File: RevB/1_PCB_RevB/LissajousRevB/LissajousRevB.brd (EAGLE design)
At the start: 99.1 x 66 mm, 77 parts, among them U101 LM348D, U201 LM348D, U401 LM348D

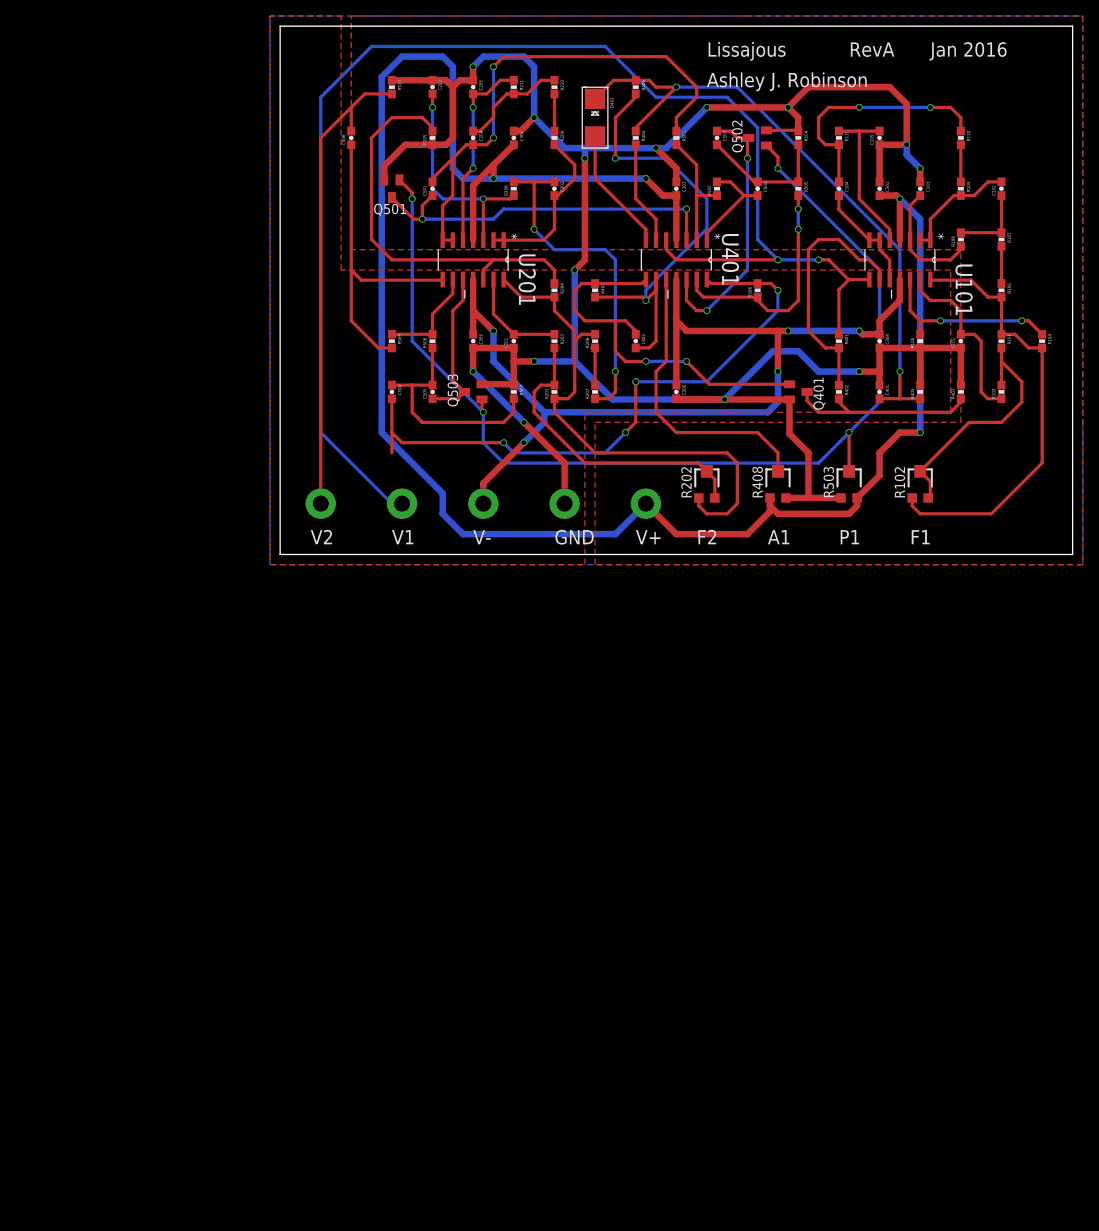
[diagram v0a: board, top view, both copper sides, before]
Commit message: down to one quad op-amp package
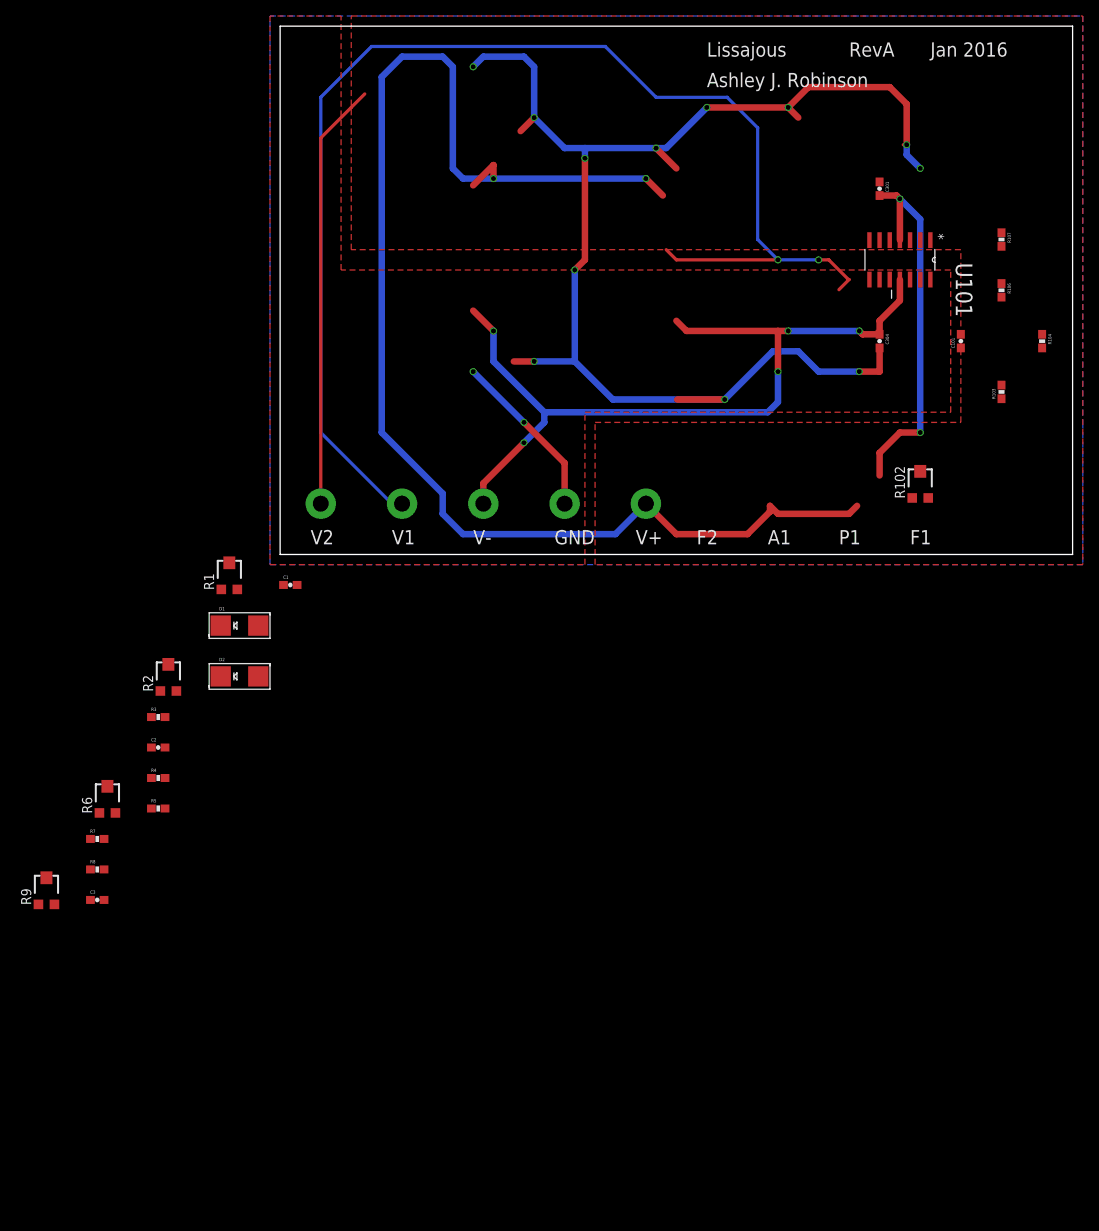
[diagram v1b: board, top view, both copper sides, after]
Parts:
- removed C102, C103, C104, C105, C201, C202, C203, C204, C205: 4.7nF, passives:0603-CAP
- removed C302, C303, C305, C306, C402: 100nF, passives:0603-CAP
- removed C401: 100pF, passives:0603-CAP
- removed C501, C502, C503, C504, C505, C506: 10nF, passives:0603-CAP
- removed D401: 1N4148, adafruit:SMADIODE
- removed Q401, Q501, Q502, Q503: (no value), adafruit:SOT23
- removed R101, R201, R403, R405, R407: DNF, passives:0603-RES
- removed R105, R108, R110, R111, R204, R205, R207, R208, R210, R211, R501, R502, R504, R505, R506, R507, R508, R509, R510: 33K, passives:0603-RES
- removed R109, R206, R209, R402: 0R, passives:0603-RES
- removed R202, R408, R503: 200K, adafruit:TC33X
- removed R203, R406: 5K6, passives:0603-RES
- removed R401: 1M, passives:0603-RES
- removed R404: 100K, passives:0603-RES
- removed U201, U401: LM348D, LM348D:SOIC127P600X175-14N
- added C1, C2, C3: 4.7nF, passives:0603-CAP
- added D1, D2: 1N4148, adafruit:SMADIODE
- added R1, R2, R6, R9: 200K, adafruit:TC33X
- added R3, R4, R5, R7, R8: 5K, passives:0603-RES
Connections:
- removed net N$11: C105.2, R111.1, U101.5
- removed net N$13: R401.2, R402.1, U101.9
- removed net N$14: R109.1, R110.2
- removed net N$16: C203.2, R208.1, U201.3
- removed net N$20: C501.1, Q501.3, U401.3
- removed net N$21: C202.2, R209.2, U201.1, U201.2
- removed net N$22: R206.1, R207.2
- removed net N$23: R209.1, R210.2
- removed net N$24: R201.2, R202.2, R202.3, R203.2
- removed net N$25: C402.2, R406.2, R407.2, U401.9
- removed net N$26: R501.2, R502.1, U401.2
- removed net N$27: R404.2, U401.6
- removed net N$28: D401.A, U401.7
- removed net N$29: C502.1, C503.2, R504.2, R505.1
- removed net N$30: C401.2, D401.C, R404.1, R405.1, R406.1
- removed net N$31: Q401.3, R402.2, R403.1
- removed net N$32: C402.1, Q401.1, R407.1, U401.8
- removed net N$33: C502.2, R502.2, U401.1
- removed net N$34: R408.2, U401.10
- removed net N$36: C503.1, Q502.3, U401.12
- removed net N$37: R505.2, R506.1, U401.13
- removed net N$38: Q501.1, Q502.1, Q503.1, R503.2
- removed net N$39: C504.2, R506.2, U401.14
- removed net N$40: R508.2, R509.1, U201.9
- removed net N$42: C504.1, C505.2, R507.2, R508.1
- removed net N$45: C505.1, Q503.3, U201.10
- removed net N$46: C506.1, R509.2, U201.8
- removed net N$6: C102.1, R107.1, R108.2
- removed net N$8: C102.2, R109.2, U101.1, U101.2
- removed net SINEGEN1: C104.2, U101.10, U101.6, U101.7
- removed net SINEGEN2: C204.2, C501.2, R501.1, U201.6, U201.7
- new net SINE: D1.C, D2.A, R103.1, R106.1, U101.14, U101.3
- net 0V: now also R102.1, R102.2, R107.2, R3.2; no longer C103.1, C105.1, C201.1, C203.1, C205.1, C302.1, C303.1, C305.2, C306.2, C401.1, Q401.2, Q501.2, Q502.2, Q503.2, R105.1, R205.1, R403.2, R405.2, R408.3, R503.1, R504.1, R507.1, R510.1
- net N$1: now also R1.3, R103.2; no longer C101.2, R103.1, U101.13
- net N$10: now also C2.1, R6.3, U101.5; no longer C201.2, R203.1, U201.13
- net N$12: now also C2.2, R2.2, R2.3, R4.2, U101.1; no longer C104.1, R110.1, R111.2
- net N$15: now also R7.1, R8.2, U101.9; no longer R201.1, R202.1, R204.2, R206.2, U201.14
- net N$17: now also C3.1, R9.3, U101.10; no longer C202.1, R207.1, R208.2
- net N$18: now also R8.1, U101.8; no longer C205.2, R211.1, U201.5
- net N$19: now also C3.2, R5.1, R7.2, U101.7; no longer C204.1, R210.1, R211.2
- net N$2: now also R102.3; no longer R105.2, U101.12
- net N$3: now also D1.A, D2.C, R106.2, R107.1, U101.13; no longer R106.1, R107.2
- net N$4: now also C1.2, R1.1, R1.2; no longer R101.2, R102.2, R102.3, R103.2
- net N$5: now also R2.1, R3.1, U101.2; no longer C103.2, R108.1, U101.3
- net N$7: now also C1.1, C101.2, U101.12; no longer R101.1, R102.1, R106.2, U101.14
- net N$9: now also R4.1, R5.2, U101.6; no longer R204.1, R205.2, U201.12
- net V+: no longer C302.2, C303.2, R408.1, R503.3, U201.4, U401.4
- net V-: no longer C305.1, C306.1, U201.11, U401.11
- net VIEW1: no longer R401.1, U101.8, U401.5
- net VIEW2: no longer C506.2, R510.2
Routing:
- net N$38: track 135.5 -> 0.00 mm, vias 4 -> 0
- net 0V: track 307.7 -> 192.7 mm
- net N$30: track 79.1 -> 0.00 mm, vias 2 -> 0
- net N$39: track 78.4 -> 0.00 mm, vias 4 -> 0
- net SINEGEN2: track 65.1 -> 0.00 mm, vias 2 -> 0
- net N$15: track 64.9 -> 0.00 mm
- net N$25: track 58.7 -> 0.00 mm, vias 2 -> 0
- net N$7: track 54.9 -> 0.00 mm
- net N$9: track 51.4 -> 0.00 mm
- net N$32: track 48.4 -> 0.00 mm, vias 2 -> 0
- net N$20: track 46.2 -> 0.00 mm, vias 2 -> 0
- net N$17: track 42.2 -> 0.00 mm, vias 2 -> 0
- net N$46: track 40.5 -> 0.00 mm
- net N$24: track 38.5 -> 0.00 mm
- net N$34: track 37.1 -> 0.00 mm
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
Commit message: core schematics done
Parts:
- removed TO304, TP301, TP302, TP303, TP305: PAD, pad:PAD
- added R22: 10K, passives:0603-RES
- C11, C12: value 4.7nF -> 820pF
- C31, C41: value 4.7nF -> 1.5nF
- R12: value 5K -> 15K
- R13: value 33K -> 15K
- R15: value 0R -> 100K
- R16: value 33K -> 47K
- R21, R31, R32, R41, R42: value 5K -> 10K
- renumbered C1 to C11, C101 to C12, C2 to C31, C3 to C41, D1 to D11, D2 to D12, R1 to R11, R102 to R14, R103 to R12, R104 to R13, R106 to R15, R107 to R16, R2 to R23, R3 to R21, R4 to R31, R5 to R32, R6 to R33, R7 to R41, R8 to R42, R9 to R43, U101 to U1
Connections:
- removed net N$5: R21.1, R23.1, U1.2
- removed net VIEW1: TO304.P$2
- removed net VIEW2: TP305.P$2
- new net N$6: R22.1, R23.1
- new net N$8: R21.1, R22.2, U1.2
- net 0V: now also R33.1, R33.2, R43.1, R43.2; no longer TP303.P$2
- net V+: no longer TP301.P$2
- net V-: no longer TP302.P$2
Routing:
- net V+: track 219.7 -> 47.1 mm, vias 4 -> 2
- net VIEW1: track 161.0 -> 0.00 mm, vias 2 -> 0
- net VIEW2: track 53.5 -> 0.00 mm
- net 0V: track 192.7 -> 171.5 mm, vias 14 -> 12
- net V-: track 103.6 -> 101.1 mm

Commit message: ready to route
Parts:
- added AMP, GND1, GND2, OUT, SINE, V1+, V1-, V2+, V2-: TESTPADS, TestPads:TEST
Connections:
- net 0V: now also GND1.1, GND2.1
- net N$12: now also AMP.1
- net N$18: now also OUT.1
- net SINE: now also SINE.1
- net V+: now also V1+.1, V2+.1
- net V-: now also V1-.1, V2-.1
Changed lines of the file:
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@@
 <wire x1="99.06" y1="66.04" x2="0" y2="66.04" width="0" layer="20"/>
 <text x="13.97" y="1.27" size="1.778" layer="21">V1</text>
-<text x="3.81" y="1.27" size="1.778" layer="21">V2</text>
+<text x="5.08" y="11.43" size="1.778" layer="21">V2</text>
 <text x="44.45" y="1.27" size="1.778" layer="21">V+</text>
 <text x="34.29" y="1.27" size="1.778" layer="21">GND</text>
@@
 <wire x1="36.576" y1="7.366" x2="36.576" y2="5.334" width="0.0762" layer="144"/>
 <wire x1="36.576" y1="5.334" x2="35.56" y2="6.35" width="0.0762" layer="144"/>
-<wire x1="4.064" y1="6.35" x2="5.08" y2="6.35" width="0.0762" layer="144"/>
-<wire x1="5.08" y1="6.35" x2="6.096" y2="7.366" width="0.0762" layer="144"/>
-<wire x1="6.096" y1="7.366" x2="6.096" y2="5.334" width="0.0762" layer="144"/>
-<wire x1="6.096" y1="5.334" x2="5.08" y2="6.35" width="0.0762" layer="144"/>
 <wire x1="37.084" y1="48.514" x2="39.116" y2="50.546" width="0.0762" layer="144"/>
 <wire x1="37.084" y1="50.546" x2="39.116" y2="48.514" width="0.0762" layer="144"/>
@@
 <element name="R43" library="adafruit" package="TC33X" value="200K" x="-29.21" y="-41.91"/>
 <element name="R22" library="passives" package="0603-RES" value="10K" x="-30.48" y="-46.99"/>
+<element name="V1+" library="TestPads" package="TEST" value="TESTPADS" x="-29.21" y="-50.8"/>
+<element name="GND1" library="TestPads" package="TEST" value="TESTPADS" x="-29.21" y="-54.61"/>
+<element name="V1-" library="TestPads" package="TEST" value="TESTPADS" x="-29.21" y="-58.42"/>
+<element name="V2+" library="TestPads" package="TEST" value="TESTPADS" x="-29.21" y="-62.23"/>
+<element name="GND2" library="TestPads" package="TEST" value="TESTPADS" x="-29.21" y="-66.04"/>
+<element name="V2-" library="TestPads" package="TEST" value="TESTPADS" x="-29.21" y="-69.85"/>
+<element name="SINE" library="TestPads" package="TEST" value="TESTPADS" x="-29.21" y="-73.66"/>
+<element name="AMP" library="TestPads" package="TEST" value="TESTPADS" x="-29.21" y="-77.47"/>
+<element name="OUT" library="TestPads" package="TEST" value="TESTPADS" x="-29.21" y="-81.28"/>
 </elements>
 <signals>
@@
 <vertex x="-1.27" y="-1.27"/>
 </polygon>
+<contactref element="V1-" pad="1"/>
+<contactref element="V2-" pad="1"/>
+<wire x1="-29.21" y1="-58.42" x2="-29.21" y2="-69.85" width="0" layer="19" extent="1-1"/>
+<wire x1="25.4" y1="8.89" x2="-29.21" y2="-58.42" width="0" layer="19" extent="1-1"/>
 </signal>
 <signal name="V+">
@@
 <vertex x="100.33" y="-1.27"/>
 </polygon>
+<contactref element="V1+" pad="1"/>
+<contactref element="V2+" pad="1"/>
+<wire x1="-29.21" y1="-50.8" x2="-29.21" y2="-62.23" width="0" layer="19" extent="1-1"/>
+<wire x1="74.93" y1="9.875" x2="-29.21" y2="-50.8" width="0" layer="19" extent="1-1"/>
 </signal>
 <signal name="0V">
@@
 <contactref element="R43" pad="2"/>
 <contactref element="R21" pad="2"/>
+<contactref element="GND1" pad="1"/>
+<contactref element="GND2" pad="1"/>
 <wire x1="85.09" y1="25.82" x2="90.17" y2="38.52" width="0" layer="19" extent="1-1"/>
 <wire x1="74.93" y1="25.82" x2="85.09" y2="25.82" width="0" layer="19" extent="1-1"/>
@@
 <wire x1="-29.21" y1="-40.41" x2="-22.59" y2="-32.305" width="0" layer="19" extent="1-1"/>
 <wire x1="-30.21" y1="-43.735" x2="-29.21" y2="-40.41" width="0" layer="19" extent="1-1"/>
+<wire x1="-29.21" y1="-54.61" x2="-30.21" y2="-43.735" width="0" layer="19" extent="1-1"/>
+<wire x1="-29.21" y1="-66.04" x2="-29.21" y2="-54.61" width="0" layer="19" extent="1-1"/>
 </signal>
 <signal name="N$2">
@@
 <contactref element="D12" pad="A"/>
 <contactref element="U1" pad="3"/>
+<contactref element="SINE" pad="1"/>
 <wire x1="81.28" y1="34.3662" x2="90.17" y2="33.87" width="0" layer="19" extent="1-1"/>
 <wire x1="78.74" y1="39.2938" x2="81.28" y2="34.3662" width="0" layer="19" extent="1-1"/>
@@
 <wire x1="-2.7305" y1="-15.24" x2="81.28" y2="34.3662" width="0" layer="19" extent="1-1"/>
 <wire x1="-7.4295" y1="-8.89" x2="-2.7305" y2="-15.24" width="0" layer="19" extent="1-1"/>
+<wire x1="-29.21" y1="-73.66" x2="-2.7305" y2="-15.24" width="0" layer="19" extent="1-1"/>
 </signal>
 <signal name="N$3">
@@
 <contactref element="U1" pad="8"/>
 <contactref element="R42" pad="1"/>
-<wire x1="-23.71" y1="-39.37" x2="73.66" y2="34.3662" width="0" layer="19" extent="1-1"/>
+<contactref element="OUT" pad="1"/>
+<wire x1="-23.71" y1="-39.37" x2="-29.21" y2="-81.28" width="0" layer="19" extent="1-1"/>
+<wire x1="73.66" y1="34.3662" x2="-23.71" y2="-39.37" width="0" layer="19" extent="1-1"/>
 </signal>
 <signal name="N$19">
@@
 <contactref element="R23" pad="3"/>
 <contactref element="R23" pad="2"/>
+<contactref element="AMP" pad="1"/>
 <wire x1="-13.97" y1="-13.74" x2="81.28" y2="39.2938" width="0" layer="19" extent="1-1"/>
 <wire x1="-12.97" y1="-17.065" x2="-13.97" y2="-13.74" width="0" layer="19" extent="1-1"/>
 <wire x1="-14.39" y1="-24.13" x2="-12.97" y2="-17.065" width="0" layer="19" extent="1-1"/>
 <wire x1="-14.39" y1="-27.94" x2="-14.39" y2="-24.13" width="0" layer="19" extent="1-1"/>
+<wire x1="-29.21" y1="-77.47" x2="-14.39" y2="-27.94" width="0" layer="19" extent="1-1"/>
 </signal>
 <signal name="N$6">

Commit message: initial placement
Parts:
- removed C301, C304: 100nF, passives:0603-CAP
- added C51, C52: 100nF, passives:0603-CAP
- added GND3, GND4, GND5: TESTPADS, TestPads:TEST
- moved OUT 149.0 mm to (54.6, 41.9)
- moved AMP 133.7 mm to (54.6, 26.7)
- moved V1- 129.3 mm to (14.0, 63.5), turned to 90 degrees
- moved GND1 124.1 mm to (8.89, 63.5), turned to 90 degrees
- moved SINE 119.4 mm to (54.6, 11.4)
- moved V1+ 119.0 mm to (3.81, 63.5), turned to 90 degrees
- moved R43 110.6 mm to (33.0, 49.5)
- moved R42 102.9 mm to (41.9, 40.6), turned to 270 degrees
- moved R22 102.6 mm to (22.9, 40.6), turned to 270 degrees
- moved C41 101.4 mm to (34.3, 40.6), turned to 90 degrees
- moved R41 97.6 mm to (38.1, 40.6), turned to 90 degrees
- moved V2- 84.3 mm to (14.0, 2.54), turned to 90 degrees
- moved R15 79.4 mm to (11.4, 22.9)
- moved R32 79.0 mm to (41.9, 22.9), turned to 270 degrees
- moved GND2 78.5 mm to (8.89, 2.54), turned to 90 degrees
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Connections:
- net 0V: now also C51.1, C52.2, GND3.1, GND4.1, GND5.1; no longer C301.1, C304.2
- net V+: now also C51.2; no longer C301.2
- net V-: now also C52.1; no longer C304.1
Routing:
- net 0V: track 171.5 -> 0.00 mm, vias 12 -> 0
- net V-: track 101.1 -> 0.00 mm, vias 5 -> 0
- net V+: track 47.1 -> 0.00 mm, vias 2 -> 0
- removed copper zone on layer 16, net 0V
- removed copper zone on layer 1, net V+
- removed copper zone on layer 1, net V-
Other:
- board size 99.1 x 66 mm -> 57.1 x 66 mm
- board text removed: "0.6000 mm / 23.622 mil"
- board text removed: "2.0000 mm / 78.740 mil"
- board text removed: "A1"
- board text removed: "Date: 09/01/2016 13:42"
- board text removed: "Drill legend"
- board text removed: "F1"
- board text removed: "F2"
- board text removed: "GND"
- board text removed: "P1"
- board text removed: "V+"
- board text removed: "V-"
- board text removed: "V1"
- board text removed: "V2"
